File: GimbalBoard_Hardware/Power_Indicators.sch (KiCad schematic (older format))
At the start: 8 parts

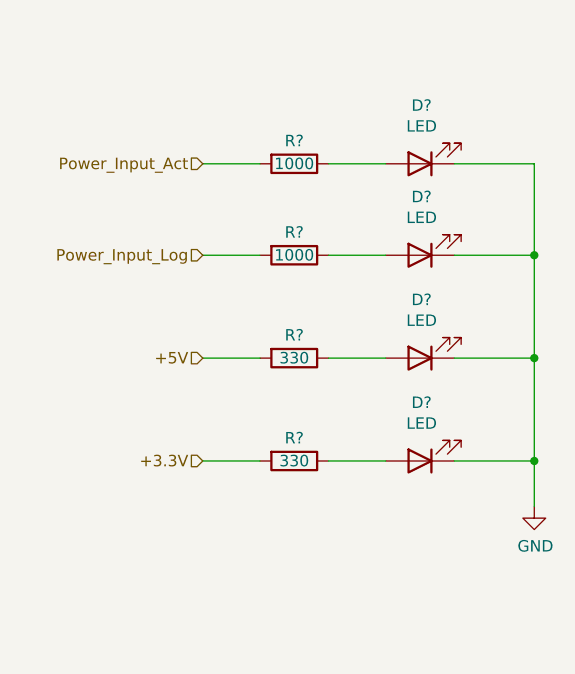
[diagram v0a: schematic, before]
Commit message: connected everything up and changed power to accomodate teensy instead of tiva
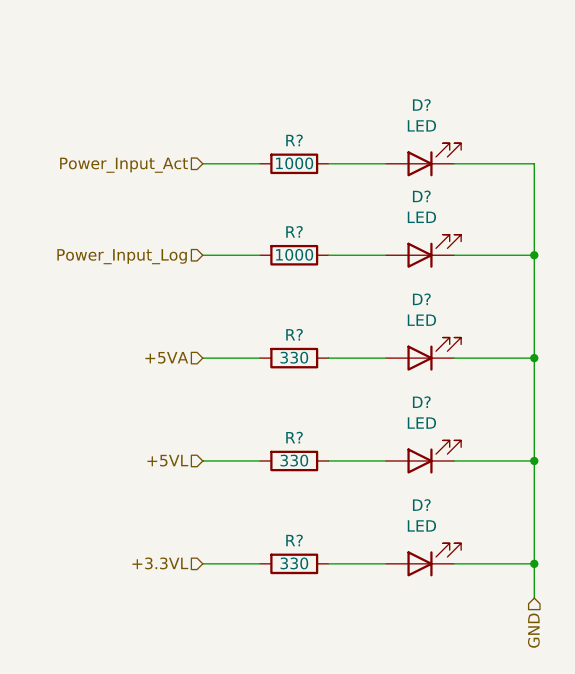
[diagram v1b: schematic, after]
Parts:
- added D?: LED, symbol Device:LED
- added R?: 330, symbol Device:R
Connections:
- net GND: now also D?.1 (K)
- net +3.3V renamed +5VL
- net +5V renamed +5VA
- new net: D?.2 (A), R?.1
- new net +3.3VL: R?.2
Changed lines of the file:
@@
 $Descr A4 11693 8268
 encoding utf-8
-Sheet 5 7
+Sheet 5 8
 Title ""
 Date ""
@@
 	0    1    1    0
 $EndComp
-$Comp
-L power:GND #PWR?
-U 1 1 61618B06
-P 5900 5000
-F 0 "#PWR?" H 5900 4750 50  0001 C CNN
-F 1 "GND" H 5905 4827 50  0000 C CNN
-F 2 "" H 5900 5000 50  0001 C CNN
-F 3 "" H 5900 5000 50  0001 C CNN
-	1    5900 5000
-	1    0    0    -1
-$EndComp
 Text HLabel 4450 3500 0    50   Input ~ 0
 Power_Input_Act
@@
 Power_Input_Log
 Text HLabel 4450 4350 0    50   Input ~ 0
-+5V
++5VA
 Text HLabel 4450 4800 0    50   Input ~ 0
-+3.3V
++5VL
 Wire Wire Line
 	4450 4800 4700 4800
@@
 Wire Wire Line
 	5550 4800 5900 4800
-Wire Wire Line
-	5900 4800 5900 5000
 Wire Wire Line
 	4450 3500 4700 3500
@@
 Wire Wire Line
 	5900 4350 5900 4800
+$Comp
+L Device:LED D?
+U 1 1 6168B9D3
+P 5400 5250
+F 0 "D?" H 5393 4995 50  0000 C CNN
+F 1 "LED" H 5393 5086 50  0000 C CNN
+F 2 "" H 5400 5250 50  0001 C CNN
+F 3 "~" H 5400 5250 50  0001 C CNN
+	1    5400 5250
+	-1   0    0    1
+$EndComp
+$Comp
+L Device:R R?
+U 1 1 6168B9D9
+P 4850 5250
+F 0 "R?" V 4750 5250 50  0000 C CNN
+F 1 "330" V 4850 5250 50  0000 C CNN
+F 2 "" V 4780 5250 50  0001 C CNN
+F 3 "~" H 4850 5250 50  0001 C CNN
+	1    4850 5250
+	0    1    1    0
+$EndComp
+Text HLabel 4450 5250 0    50   Input ~ 0
++3.3VL
+Wire Wire Line
+	4450 5250 4700 5250
+Wire Wire Line
+	5000 5250 5250 5250
+Wire Wire Line
+	5550 5250 5900 5250
+Wire Wire Line
+	5900 4800 5900 5250
+Connection ~ 5900 5250
+Wire Wire Line
+	5900 5250 5900 5400
+Text HLabel 5900 5400 3    50   Input ~ 0
+GND
 $EndSCHEMATC

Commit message: added more text
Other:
- note added: "Power Indicators"
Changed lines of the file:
@@
 $Descr A4 11693 8268
 encoding utf-8
-Sheet 5 8
+Sheet 8 8
 Title ""
 Date ""
@@
 Text HLabel 5900 5400 3    50   Input ~ 0
 GND
+Text Notes 4600 3000 0    79   ~ 0
+Power Indicators
 $EndSCHEMATC

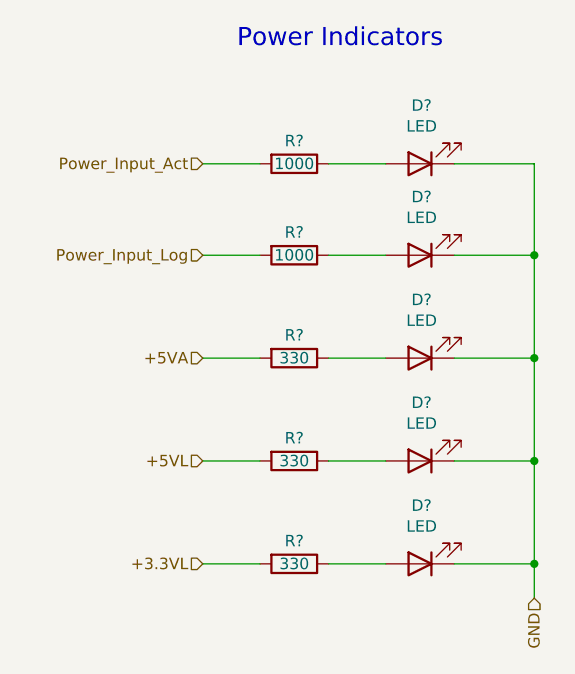
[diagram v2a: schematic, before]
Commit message: added labels, numbered everything, added no connection to pins. Still can't get past a couple pf errors in the electrical rules check
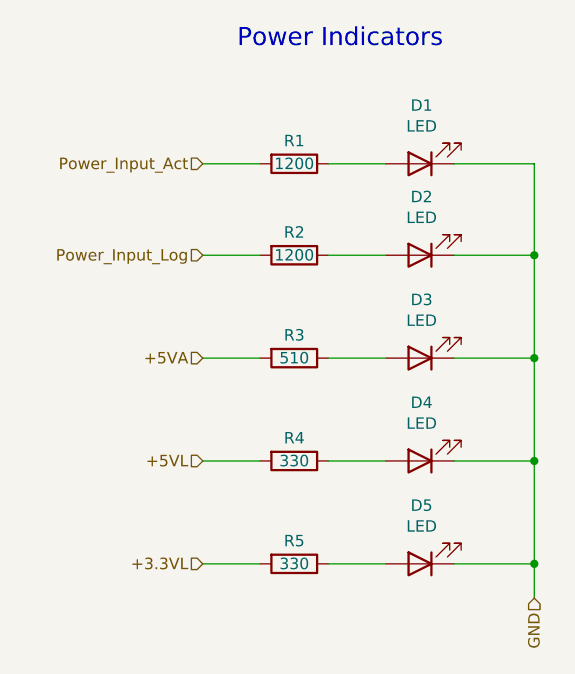
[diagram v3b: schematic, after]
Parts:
- R1, R2: renamed from R?; value 1000 -> 1200
- R3: renamed from R?; value 330 -> 510
- gave numbers to parts that had none: 7
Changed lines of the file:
@@
 $EndDescr
 $Comp
-L Device:LED D?
+L Device:LED D1
 U 1 1 61616BF1
 P 5400 3500
-F 0 "D?" H 5393 3245 50  0000 C CNN
+F 0 "D1" H 5393 3245 50  0000 C CNN
 F 1 "LED" H 5393 3336 50  0000 C CNN
 F 2 "" H 5400 3500 50  0001 C CNN
@@
 $EndComp
 $Comp
-L Device:LED D?
+L Device:LED D2
 U 1 1 616170E3
 P 5400 3900
-F 0 "D?" H 5393 3645 50  0000 C CNN
+F 0 "D2" H 5393 3645 50  0000 C CNN
 F 1 "LED" H 5393 3736 50  0000 C CNN
 F 2 "" H 5400 3900 50  0001 C CNN
@@
 $EndComp
 $Comp
-L Device:LED D?
+L Device:LED D3
 U 1 1 61617421
 P 5400 4350
-F 0 "D?" H 5393 4095 50  0000 C CNN
+F 0 "D3" H 5393 4095 50  0000 C CNN
 F 1 "LED" H 5393 4186 50  0000 C CNN
 F 2 "" H 5400 4350 50  0001 C CNN
@@
 $EndComp
 $Comp
-L Device:LED D?
+L Device:LED D4
 U 1 1 61617697
 P 5400 4800
-F 0 "D?" H 5393 4545 50  0000 C CNN
+F 0 "D4" H 5393 4545 50  0000 C CNN
 F 1 "LED" H 5393 4636 50  0000 C CNN
 F 2 "" H 5400 4800 50  0001 C CNN
@@
 $EndComp
 $Comp
-L Device:R R?
+L Device:R R1
 U 1 1 616177E3
 P 4850 3500
-F 0 "R?" V 4750 3500 50  0000 C CNN
-F 1 "1000" V 4850 3500 50  0000 C CNN
+F 0 "R1" V 4750 3500 50  0000 C CNN
+F 1 "1200" V 4850 3500 50  0000 C CNN
 F 2 "" V 4780 3500 50  0001 C CNN
 F 3 "~" H 4850 3500 50  0001 C CNN
@@
 $EndComp
 $Comp
-L Device:R R?
+L Device:R R2
 U 1 1 61617F3E
 P 4850 3900
-F 0 "R?" V 4750 3900 50  0000 C CNN
-F 1 "1000" V 4850 3900 50  0000 C CNN
+F 0 "R2" V 4750 3900 50  0000 C CNN
+F 1 "1200" V 4850 3900 50  0000 C CNN
 F 2 "" V 4780 3900 50  0001 C CNN
 F 3 "~" H 4850 3900 50  0001 C CNN
@@
 $EndComp
 $Comp
-L Device:R R?
+L Device:R R3
 U 1 1 616181AB
 P 4850 4350
-F 0 "R?" V 4750 4350 50  0000 C CNN
-F 1 "330" V 4850 4350 50  0000 C CNN
+F 0 "R3" V 4750 4350 50  0000 C CNN
+F 1 "510" V 4850 4350 50  0000 C CNN
 F 2 "" V 4780 4350 50  0001 C CNN
 F 3 "~" H 4850 4350 50  0001 C CNN
@@
 $EndComp
 $Comp
-L Device:R R?
+L Device:R R4
 U 1 1 616183C7
 P 4850 4800
-F 0 "R?" V 4750 4800 50  0000 C CNN
+F 0 "R4" V 4750 4800 50  0000 C CNN
 F 1 "330" V 4850 4800 50  0000 C CNN
 F 2 "" V 4780 4800 50  0001 C CNN
@@
 	5900 4350 5900 4800
 $Comp
-L Device:LED D?
+L Device:LED D5
 U 1 1 6168B9D3
 P 5400 5250
-F 0 "D?" H 5393 4995 50  0000 C CNN
+F 0 "D5" H 5393 4995 50  0000 C CNN
 F 1 "LED" H 5393 5086 50  0000 C CNN
 F 2 "" H 5400 5250 50  0001 C CNN
@@
 $EndComp
 $Comp
-L Device:R R?
+L Device:R R5
 U 1 1 6168B9D9
 P 4850 5250
-F 0 "R?" V 4750 5250 50  0000 C CNN
+F 0 "R5" V 4750 5250 50  0000 C CNN
 F 1 "330" V 4850 5250 50  0000 C CNN
 F 2 "" V 4780 5250 50  0001 C CNN

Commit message: sheet has been reviewed
schematic has been reviewed. and resister values have been changed. as well as a ground being added
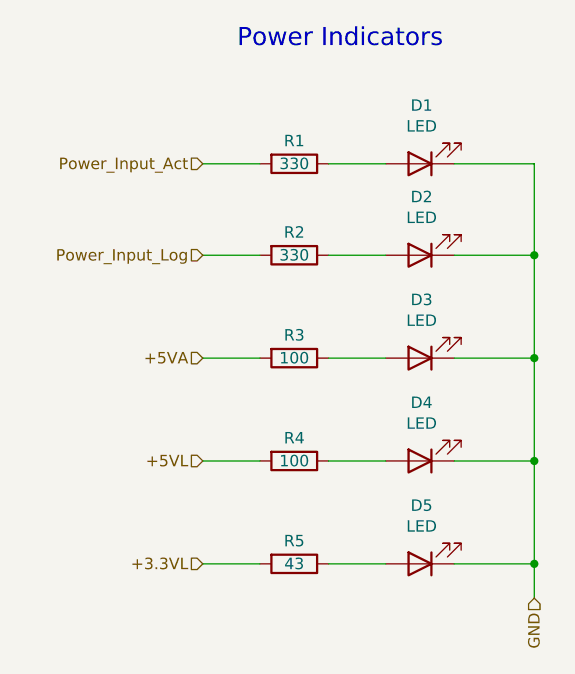
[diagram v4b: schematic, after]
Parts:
- R1, R2: value 1200 -> 330
- R3: value 510 -> 100
- R4: value 330 -> 100
- R5: value 330 -> 43
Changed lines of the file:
@@
 P 4850 3500
 F 0 "R1" V 4750 3500 50  0000 C CNN
-F 1 "1200" V 4850 3500 50  0000 C CNN
+F 1 "330" V 4850 3500 50  0000 C CNN
 F 2 "" V 4780 3500 50  0001 C CNN
 F 3 "~" H 4850 3500 50  0001 C CNN
@@
 P 4850 3900
 F 0 "R2" V 4750 3900 50  0000 C CNN
-F 1 "1200" V 4850 3900 50  0000 C CNN
+F 1 "330" V 4850 3900 50  0000 C CNN
 F 2 "" V 4780 3900 50  0001 C CNN
 F 3 "~" H 4850 3900 50  0001 C CNN
@@
 P 4850 4350
 F 0 "R3" V 4750 4350 50  0000 C CNN
-F 1 "510" V 4850 4350 50  0000 C CNN
+F 1 "100" V 4850 4350 50  0000 C CNN
 F 2 "" V 4780 4350 50  0001 C CNN
 F 3 "~" H 4850 4350 50  0001 C CNN
@@
 P 4850 4800
 F 0 "R4" V 4750 4800 50  0000 C CNN
-F 1 "330" V 4850 4800 50  0000 C CNN
+F 1 "100" V 4850 4800 50  0000 C CNN
 F 2 "" V 4780 4800 50  0001 C CNN
 F 3 "~" H 4850 4800 50  0001 C CNN
@@
 P 4850 5250
 F 0 "R5" V 4750 5250 50  0000 C CNN
-F 1 "330" V 4850 5250 50  0000 C CNN
+F 1 "43" V 4850 5250 50  0000 C CNN
 F 2 "" V 4780 5250 50  0001 C CNN
 F 3 "~" H 4850 5250 50  0001 C CNN
